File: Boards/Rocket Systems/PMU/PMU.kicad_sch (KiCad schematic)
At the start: 70 parts, among them J1 2200981271, J2 XT30UPB-F, J3 XT30UPB-F, J4 XT30UPB-F, J5 XT30UPB-F, K3 G3VM-31DR_TR05_, K4 G3VM-31DR_TR05_, K5 G3VM-31DR_TR05_, Q1 NPN, Q2 PMOS, U7 NJD35N04T4G, U8 NJD35N04T4G, U9 NJD35N04T4G

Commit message: PMU continuacíon
coisas
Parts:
- removed DSUB1: ~, HDL15-SL-B:HDL15-SL-B, symbol HDL15-SL-B:HDL15-SL-B
- added C37, C39: 4.7uF, Capacitor-0402:Capacitor_0402, symbol Device:C
- added C40, C94: 1uF, Capacitor-0402:Capacitor_0402, symbol Device:C
- added C92: 100n, Capacitor-0402:Capacitor_0402, symbol Device:C_Small
- added C93: 10n, Capacitor-0402:Capacitor_0402, symbol Device:C_Small
- added J6: Conn_01x05_Pin, symbol Connector:Conn_01x05_Pin
- added R35, R36, R37, R38, R39, R40, R41: 2k, Resistor-0603:RES_0603, symbol Device:R
- added R70, R71, R72, R73, R74: 1k, Resistor-0603:RES_0603, symbol Device:R
- added R76: 1k, Resistor-0402:RES_0402, symbol Device:R
- added U10: ST1L05APU33R, LDO ST1L05A:DFN_5APU33R_STM, symbol LDO_ST1L05A:ST1L05APU33R
- added U29: NCV8114ASN165T1G, NCV8114ASN165T1G:SOT95P275X120-5N, symbol NCV8114ASN165T1G:NCV8114ASN165T1G
- added U30: MCP6002-E/MS, MCP6002-E-MS:MSOP8_MC_MCH, symbol MCP6002-E-MS:MCP6002-E_MS
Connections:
- net +14V is gone; now on net +5V: CR11.1, CR12.1, CR3.1
- net +3.3V: now also C39.2, C92.2, C94.1, U10.2 (V0), U29.1 (IN), U29.3 (EN), U30.8 (VDD)
- net +5V: now also C37.2, C40.2, U10.3 (V1)
- net FIRE_OUT1: now also J6.1 (Pin_1)
- net FIRE_OUT2: now also J6.2 (Pin_2)
- net FIRE_OUT3: now also J6.3 (Pin_3)
- net GND: now also C37.1, C39.1, C40.1, C92.1, C93.2, C94.2, R35.1, U10.6 (GND), U10.7 (GND), U29.2 (GND), U30.4 (VSS)
- new net: R41.2, R74.1, R76.2, U30.2 (VINA-)
- new net: R40.2, R73.1, R74.2
- new net: R39.2, R72.1, R73.2
- new net: R35.2, R36.2, R70.2
- new net: R38.2, R71.1, R72.2
- new net: R37.2, R70.1, R71.2
- new net +1.65V: C93.1, U29.5 (OUT), U30.3 (VINA+)
- new net ADC: J6.4 (Pin_4), U30.6 (VINB-), U30.7 (VOUTB)
- new net BUFF IN: R76.1, U30.1 (VOUTA), U30.5 (VINB+)
- new net V0: R36.1
- new net V1: R37.1
- new net V2: R38.1
- new net V3: R39.1
- new net V4: R40.1
- new net V5: R41.1
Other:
- note added: "Conexões para o CORTEX"
- note added: "Eagle 1"
- note added: "Eagle 2"
- note added: "TO DO: Converting the continuity signal to 3V3 Redoing the reference point for the Darling Recovery Bypass (Fala com o André :)) Charging ver como é isso Trocar modulo 5V"
- note added: "Tender Descender"
- note removed: "Conexões para o Navigator"
- note removed: "TO DO: Converting the continuity signal to 3V3 Redoing the reference point for the Darling LDO 5V-3V3 DAC-ADC Continuidade passa para a elytra Recovery Bypass (Fala com o André :))"

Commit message: PMU quase
Umas adições à lib e a PMU quase finalizada
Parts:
- removed CR11, CR12, CR3: BZX84J-B10_115, BZX84J-B10-115:CR_SC-90_NEX, symbol BZX84J-B10,115:BZX84J-B10_115
- removed R9: 750, Resistor-0805:RES_0805, symbol Device:R
- added C41, C43: 10uF, Capacitor-0402:Capacitor_0402, symbol Device:C
- added C42, C44: 0.1uF, Capacitor-0402:Capacitor_0402, symbol Device:C
- added C95: 100n, Capacitor-0402:Capacitor_0402, symbol Device:C_Small
- added D10, D11: RSX301LAM30TR, Diode-Schottky_RSX301L:DIOM5026X220N, symbol RSX301L-30DDTE25:RSX301L-30DDTE25
- added F7: MF-RHT750-0, PFNF.035.2:FUS1206_24N_SCH, symbol PFNF_035_2:PFNF.035.2
- added F8, F9: MF-RHT300-0, PFNF.035.2:FUS1206_24N_SCH, symbol PFNF_035_2:PFNF.035.2
- added IC1, IC2, IC3: LM4040DIZ-4.1_NOPB, LM336BLPE325, symbol LM4040:LM4040DIZ-4.1_NOPB
- added IC4: LS1205EFD33, SON50P300X300X80-11N, symbol LS1205EFD33:LS1205EFD33
- added Q3, Q4, Q5, Q6, Q7, Q8: NPN, symbol Simulation_SPICE:NPN
- added R19, R20, R21: 220, Resistor-0805:RES_0805, symbol Device:R
- added R42, R43, R46, R49, R52, R55: 10k, Resistor-0805:RES_0805, symbol Device:R
- added R44, R47, R50, R53, R56: 100k, Resistor-0805:RES_0805, symbol Device:R
- added R45, R48, R51, R54, R57: 47k, Resistor-0805:RES_0805, symbol Device:R
- added R58: 2.1k, RES-2512 Reversed:RESC3263X80N, symbol Device:R
- PC1: renamed from PS1; value ITX0509SA-H -> JOY-IT SBC-Buck02
- R33: value 750 -> 47k
- R34: value 750 -> 100k
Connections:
- net +3.3V: now also R42.1, R43.1, R46.1, R49.1, R52.1, R55.1
- net +5V: now also R19.1, R20.1, R21.1
- net GND: now also R34.1, C41.1, C42.1, C43.1, C44.1, C95.2, IC1.3 (-), IC2.3 (-), IC3.3 (-), IC4.11 (GND), Q3.3 (E), Q4.3 (E), Q5.3 (E), Q6.3 (E), Q7.3 (E), Q8.3 (E), R44.1, R47.1, R50.1, R53.1, R56.1, R58.2; no longer PC1.1 (-Vin), R33.2, R34.2
- net V0_IN: now also R33.2
- net V1_IN: now also R45.2
- net V2_IN: now also R48.2
- net V3_IN: now also R51.2
- net V4_IN: now also R54.2
- net V5_IN: now also R57.2
- net VBAT1: now also F8.1; no longer J5.2, Q2.3 (S), R12.1
- net VBAT2: now also F9.1
- net VDC: now also J5.2, Q2.3 (S), R12.1
- net VFill: now also F7.2
- net V0 renamed V0_OUT
- net V0_OUT: now also Q3.1 (C), R42.2
- net V1 renamed V1_OUT
- net V1_OUT: now also Q4.1 (C), R43.2
- net V2 renamed V2_OUT
- net V2_OUT: now also Q5.1 (C), R46.2
- net V3 renamed V3_OUT
- net V3_OUT: now also Q6.1 (C), R49.2
- net V4 renamed V4_OUT
- net V4_OUT: now also Q7.1 (C), R52.2
- net V5 renamed V5_OUT
- net V5_OUT: now also Q8.1 (C), R55.2
- net VB1: no longer names the net of U7.1 (B)
- net VB1: now also IC1.2 (+), R19.2
- net VB2: no longer names the net of R33.1
- net VB2: now also R34.2, Q3.2 (B); no longer U8.1 (B)
- net VB3: no longer names the net of U9.1 (B)
- net VB3: now also IC3.2 (+), R21.2; no longer R34.1
- new net: Q6.2 (B), R50.2, R51.1
- new net: Q8.2 (B), R56.2, R57.1
- new net: C41.2, C42.2, D10.2 (A), D11.2 (A), IC4.10 (OUT_3), IC4.8 (OUT_1), IC4.9 (OUT_2)
- new net: Q7.2 (B), R53.2, R54.1
- new net: D11.1 (K), F9.2
- new net: Q5.2 (B), R47.2, R48.1
- new net: D10.1 (K), F8.2
- new net: IC4.5 (ILIM), R58.1
- new net: IC2.2 (+), R20.2, U8.1 (B)
- new net: C95.1, IC4.6 (SS)
- new net: Q4.2 (B), R44.2, R45.1
- new net I_ENABLE: C43.2, C44.2, F7.1, IC4.1 (IN_1), IC4.2 (IN_2), IC4.3 (IN_3), IC4.7 (EN)
- no-connect marks 0 -> 1
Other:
- note added: "Charging Module"
- note added: "Connections"
- note added: "E-match Detection"
- note added: "EMI Filter (pi filter)"
- note added: "Parachute Arming"
- note added: "Parachute Deployment"
- note added: "Power Conversion and Reference Voltages"
- note added: "TO DO: Arming Both Batteries"
- note removed: "Revise this filter"
- note removed: "TO DO: Converting the continuity signal to 3V3 Redoing the reference point for the Darling Recovery Bypass (Fala com o André :)) Charging ver como é isso Trocar modulo 5V"
- moved on the sheet: C1, C2, C3, C37, C39, C4, C40, C5, C6, C92, C93, C94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

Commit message: Update PMU.kicad_sch
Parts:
- added J7, J8: Conn_01x02_Pin, symbol Connector:Conn_01x02_Pin
- added Q10, Q12: NPN, symbol Simulation_SPICE:NPN
- added Q11, Q9: PMOS, symbol Simulation_SPICE:PMOS
- added R22, R59, R60, R62: 100k, Resistor-0805:RES_0805, symbol Device:R
- added R23, R61: 4.7k, Resistor-0805:RES_0805, symbol Device:R
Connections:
- net VDC is gone; now on net VBAT2: C3.1, C4.1, C5.1, C6.1, J5.2, L1.2, Q2.3 (S), R12.1
- net +5V: now also J7.2 (Pin_2), J8.2 (Pin_2)
- net GND: now also J7.1 (Pin_1), J8.1 (Pin_1), Q10.3 (E), Q12.3 (E), R59.1, R62.1
- net KEY_OUT: now also R23.1, R61.1
- net VBAT1: no longer PC1.2 (+Vin)
- net VBAT2: now also Q11.3 (S), Q9.3 (S), R22.1, R60.1
- net VOUT renamed VParachute
- new net: Q10.1 (C), Q9.2 (G), R22.2
- new net: Q10.2 (B), R23.2, R59.2
- new net: Q12.2 (B), R61.2, R62.2
- new net: Q11.2 (G), Q12.1 (C), R60.2
- new net VRocket: PC1.2 (+Vin), Q9.1 (D)
- new net VVegas: Q11.1 (D)
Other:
- note added: "RocketSys Arming"
- note added: "Vegas Arming"
- note removed: "TO DO: Arming Both Batteries"
- moved on the sheet: Q1, Q2, R11, R12, R13

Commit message: Update PMU.kicad_sch
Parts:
- removed J7: Conn_01x02_Pin, symbol Connector:Conn_01x02_Pin
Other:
- moved on the sheet: J8

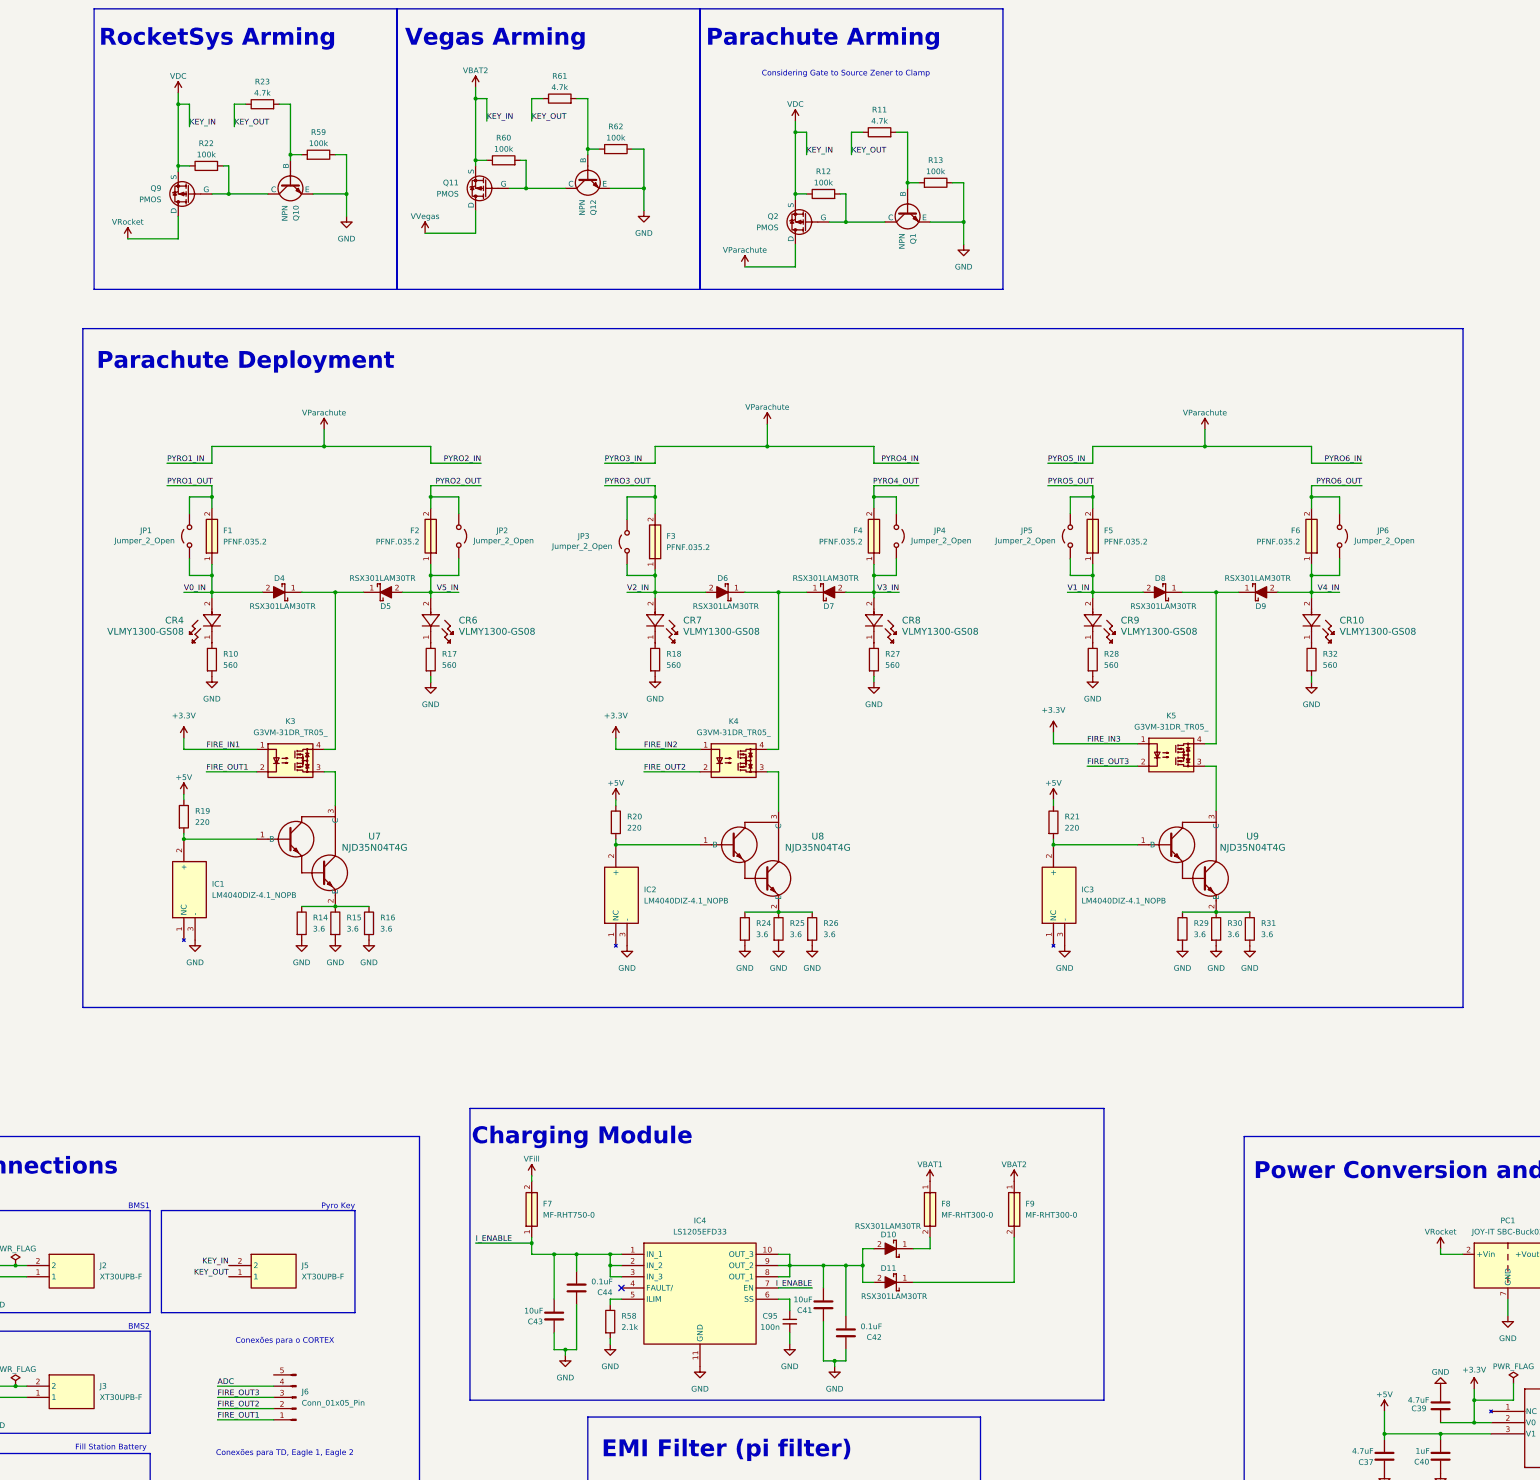
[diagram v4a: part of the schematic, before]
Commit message: PMU
Adição de várias footprints e pequenos ajustes na schematic
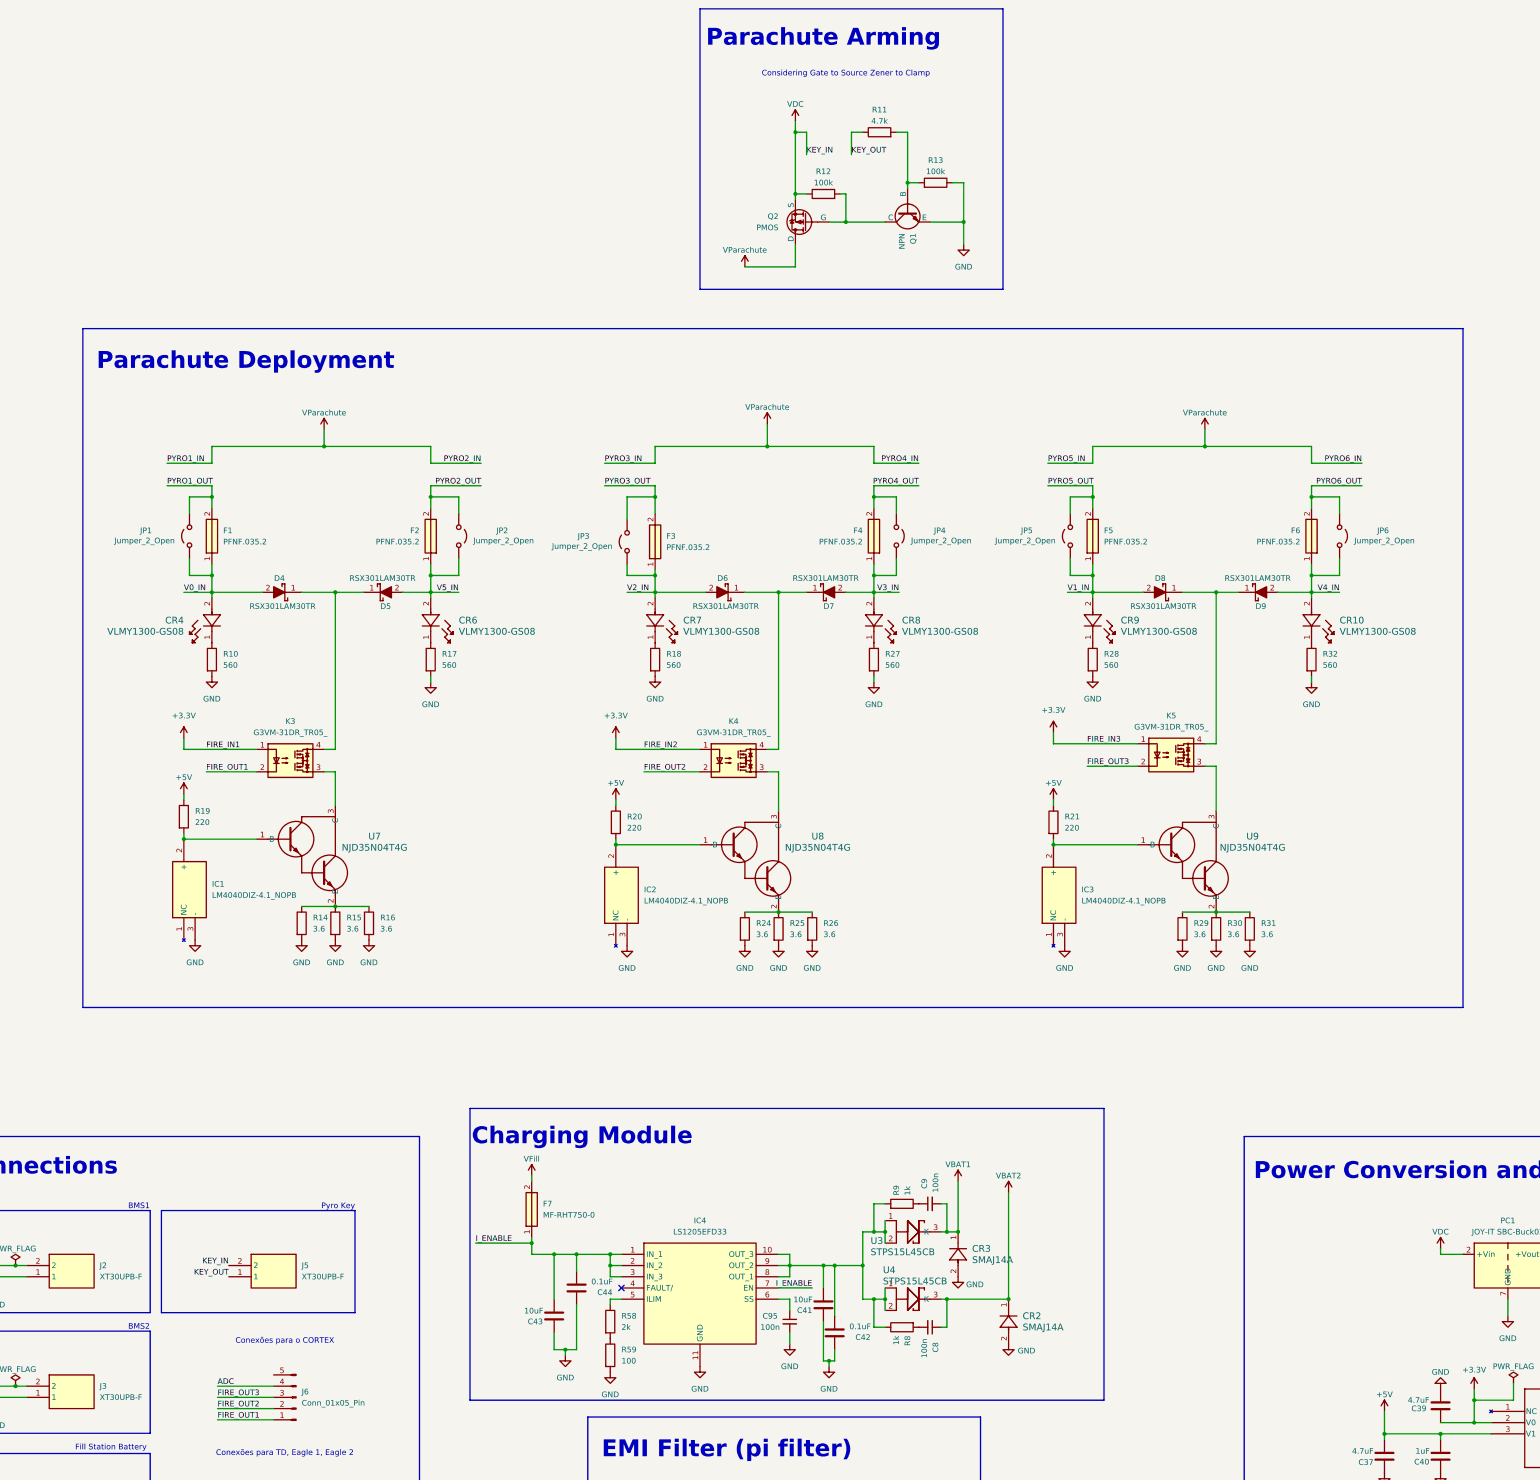
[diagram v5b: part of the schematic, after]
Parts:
- removed D10, D11: RSX301LAM30TR, Diode-Schottky_RSX301L:DIOM5026X220N, symbol RSX301L-30DDTE25:RSX301L-30DDTE25
- removed F8, F9: MF-RHT300-0, PFNF.035.2:FUS1206_24N_SCH, symbol PFNF_035_2:PFNF.035.2
- removed Q10, Q12: NPN, symbol Simulation_SPICE:NPN
- removed Q11, Q9: PMOS, symbol Simulation_SPICE:PMOS
- removed R22, R60, R62: 100k, Resistor-0805:RES_0805, symbol Device:R
- removed R23, R61: 4.7k, Resistor-0805:RES_0805, symbol Device:R
- added C8, C9: 100n, Capacitor-0603:Capacitor_0603, symbol Device:C_Small
- added CR2, CR3: SMAJ14A, SMAJ14A:SMASeries_LTF, symbol SMAJ14A:SMAJ14A
- added R8, R9: 1k, Resistor-0805:RES_0805, symbol Device:R
- added U3, U4: STPS15L45CB, STPS15L45CB:DPAK_STM, symbol STPS15L45CB:STPS15L45CB
- F7: footprint PFNF.035.2:FUS1206_24N_SCH -> MF-RHT750-0:MFRHT7500
- IC1, IC2, IC3: footprint LM336BLPE325 -> LM4040DIZ-4.1_NOPB:LM336BLPE325
- IC4: footprint SON50P300X300X80-11N -> LS1205EFD33:SON50P300X300X80-11N
- L1: footprint Inductor-2.2uH_SPM10065VT:IND_SPM10065VT-2R2M-D -> SPM10065VT-2R2M-D:SPM10065VT-2R2M-D
- Q1, Q3, Q4, Q5, Q6, Q7, Q8: footprint (none) -> BC817-40-QR:SOT95P230X110-3N
- Q2: footprint (none) -> IPD380P06NMATMA1:IPD380P06NMATMA1
- R33, R34, R42, R43, R44, R45, R46, R47, R48, R49, R50, R51, R52, R53, R54, R55, R56, R57: footprint Resistor-0805:RES_0805 -> Resistor-0603:RES_0603
- R58: value 2.1k -> 2k; footprint RES-2512 Reversed:RESC3263X80N -> Resistor-0603:RES_0603
- R59: value 100k -> 100; footprint Resistor-0805:RES_0805 -> Resistor-0603:RES_0603
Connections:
- net GND: now also R59.2, CR2.2, CR3.2; no longer R58.2, R59.1
- net VBAT1: now also C9.2, CR3.1, U3.3 (K)
- net VBAT2: now also C8.1, CR2.1, U4.3 (K); no longer C3.1, C4.1, C5.1, C6.1, J5.2, L1.2, Q2.3 (S), R12.1
- net at C41.2, C42.2, IC4.10 (OUT_3)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: now also R8.1, R9.2, U3.1, U3.2, U4.1, U4.2
- net VRocket renamed VDC
- net VDC: now also C3.1, C4.1, C5.1, C6.1, J5.2, L1.2, Q2.3 (S), R12.1
- new net: R58.2, R59.1
- new net: C8.2, R8.2
- new net: C9.1, R9.1
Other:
- note removed: "RocketSys Arming"
- note removed: "Vegas Arming"
- moved on the sheet: C42

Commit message: PMU BROW BROW
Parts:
- removed J6: Conn_01x05_Pin, symbol Connector:Conn_01x05_Pin
- added J7: Conn_01x04_Pin, symbol Connector:Conn_01x04_Pin
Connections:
- net ADC: now also J7.4 (Pin_4)
- net FIRE_OUT1: now also J7.1 (Pin_1)
- net FIRE_OUT2: now also J7.2 (Pin_2)
- net FIRE_OUT3: now also J7.3 (Pin_3)
- net V1_OUT: now also R40.1; no longer R37.1
- net V4_OUT: now also R41.1; no longer R40.1
- net V5_OUT: now also R37.1; no longer R41.1
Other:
- moved on the sheet: C94, R35, R37, R38, R39, R40, R41, R70, R71, R72, R73, R74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
